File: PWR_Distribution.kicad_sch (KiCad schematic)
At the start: 39 parts, among them IC4 AP64501QSP-13, J1 CarPowerConnector, U7 LM76202QPWPRQ1

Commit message: small changes for ravi
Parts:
- removed C36, C37, C38, C39, C40, C41: 10u 35v, Capacitor_SMD:C_0805_2012Metric, symbol Device:C
- D10: value 3.3V -> 5V
- D11: Color Green -> Red; Inventory Y -> (none); Mouser Part Number 604-APTD2012LCGCK -> 604-APTD2012LSURCK; Mouser Price/Stock https://www.mouser.com/ProductDetail/Kingbright/APTD2012LCG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 -> https://www.mouser.com/ProductDetail/Kingbright/APTD2012LSU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; P/N APTD2012LCGCK -> APTD2012LSURCK; Vf 1.9V -> 1.75V
- R45: value 2.2k -> 1.5 k
- R46: value 5k -> 5.5k
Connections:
- net GNDPWR is gone; now on net GND: J1.2 (GND)
- net +5V_PWR: no longer R41.1
- net 12V_Extn renamed +12V_EXT
- net +12V_EXT: now also R41.1

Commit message: some stuff
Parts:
- C14: value 47uF -> 10u; P/N (none) -> TMK212BBJ106MGHT
- C54: value 100nF -> 100n; Mouser Part Number 80-C0805C104M5R -> (none)
- C55: value 47uF -> 10u
- D3: Mouser Part Number 771-PESD15VL1BA-T/R -> (none); Mouser Price/Stock https://www.mouser.com/ProductDetail/Nexperia/PESD15VL1BA11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 -> (none)
- D9: value 12V -> 12V Green LED; If 2mA -> (none); Inventory Y -> (none); Mouser Part Number 604-APTD2012LCGCK -> (none); Mouser Price/Stock https://www.mouser.com/ProductDetail/Kingbright/APTD2012LCG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 -> (none); Vf 1.9V -> (none)
- R40: value 10K -> 1k; Mouser Part Number 71-CRCW080510K0FKEAC -> (none)
- R41: value 10K -> 10k; Mouser Part Number 71-CRCW080510K0FKEAC -> (none)
- R42, R7: Mouser Part Number 71-CRCW0805100KFKEAC -> (none)
- R43: value 7.5K -> 6.6k; Mouser Part Number 71-CRCW080510K0FKEAC -> (none); P/N CRCW080510K0FKEAC -> (none)
- R44: Inventory Y -> (none); Mouser Part Number 71-CRCW0805-22.1K-E3 -> (none); Mouser Price/Stock https://www.mouser.com/ProductDetail/Vishay-Dale/CRCW080522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 -> (none); P/N CRCW080522K1FKEA -> (none)
- R8: value 3k -> 200; P/N (none) -> CR0805-JW-201ELF
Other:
- note added: "Est. max power draw = 15W (pi) + 3 * (1.5W) (USB lines) + 1.5W (HDMI) + 0.6W (CAN) = 21.6W (rest of board draws negligible power)"

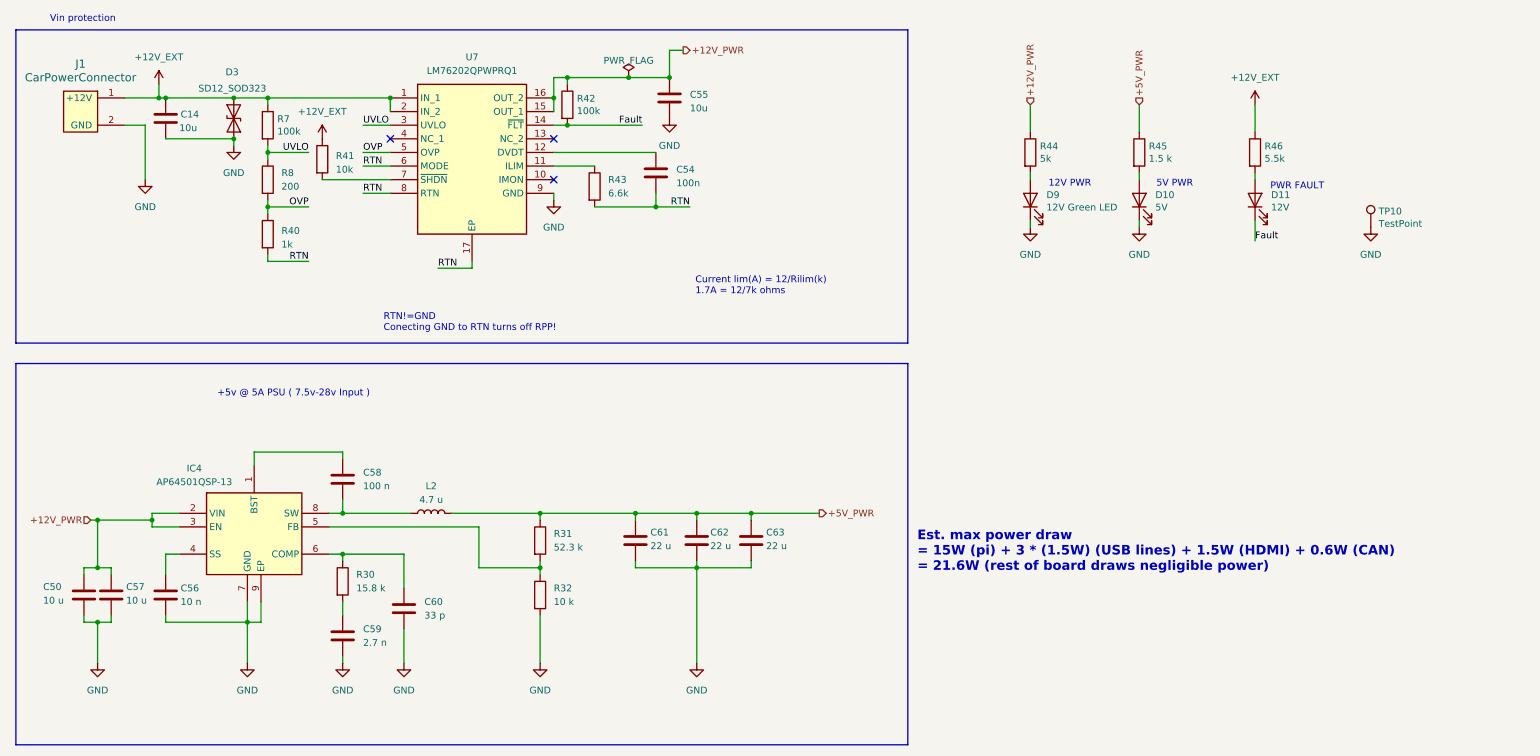
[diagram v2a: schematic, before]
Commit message: added parts to almost everything (except can xtal and fuses)
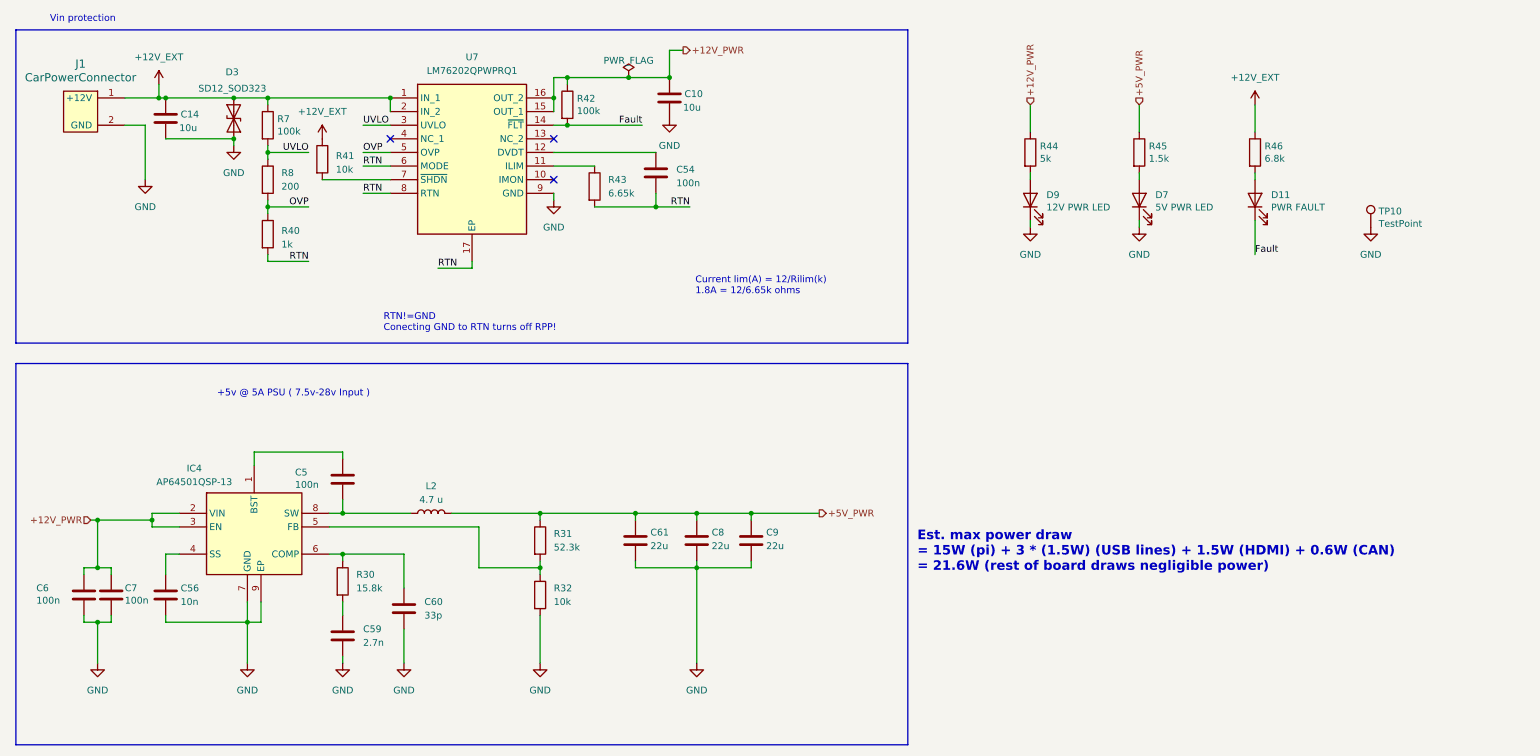
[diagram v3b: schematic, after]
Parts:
- removed C50, C57: 10 u, symbol Device:C
- removed C55: 10u, Capacitor_SMD:C_0805_2012Metric, symbol Device:C
- removed C58: 100 n, symbol Device:C
- removed C62, C63: 22 u, symbol Device:C
- removed D10: 5V, LED_SMD:LED_0805_2012Metric, symbol Device:LED
- added C10: 10u, Capacitor_SMD:C_0805_2012Metric, symbol Device:C
- added C5, C6, C7: 100n, Capacitor_SMD:C_0805_2012Metric, symbol Device:C
- added C8, C9: 22u, Capacitor_SMD:C_0805_2012Metric, symbol Device:C
- added D7: 5V PWR LED, LED_SMD:LED_0805_2012Metric, symbol Device:LED
- C56: value 10 n -> 10n; footprint (none) -> Capacitor_SMD:C_0805_2012Metric; P/N (none) -> C0805C103J5RACTU
- C59: value 2.7 n -> 2.7n; footprint (none) -> Capacitor_SMD:C_0805_2012Metric; P/N (none) -> VJ0805A272JXAAT
- C60: value 33 p -> 33p; footprint (none) -> Capacitor_SMD:C_0402_1005Metric; P/N (none) -> VJ0402A330JXACW1BC
- C61: value 22 u -> 22u; footprint (none) -> Capacitor_SMD:C_0805_2012Metric; P/N (none) -> CL21A226KQCLRNC
- D11: value 12V -> PWR FAULT; Color Red -> (none); If 2mA -> (none); Mouser Part Number 604-APTD2012LSURCK -> (none); Mouser Price/Stock https://www.mouser.com/ProductDetail/Kingbright/APTD2012LSU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 -> (none); Vf 1.75V -> (none)
- D9: value 12V Green LED -> 12V PWR LED; Color Green -> (none)
- IC4: footprint SOIC127P600X163-9N -> Controls_Pi:SOIC127P600X163-9N; Height 1.63 -> (none); Manufacturer_Name Diodes Incorporated -> (none); Manufacturer_Part_Number AP64501QSP-13 -> (none); Mouser Part Number 621-AP64501QSP-13 -> (none); Mouser Price/Stock https://www.mouser.co.uk/ProductDetail/Diodes-Incorporated/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 -> (none); P/N (none) -> AP64501QSP-13
- R30: value 15.8 k -> 15.8k; footprint (none) -> Resistor_SMD:R_0603_1608Metric; P/N (none) -> CRCW060315K8FKEAC
- R31: value 52.3 k -> 52.3k; footprint (none) -> Resistor_SMD:R_0603_1608Metric; P/N (none) -> CRCW060352K3FKEA
- R32: value 10 k -> 10k; footprint (none) -> Resistor_SMD:R_0805_2012Metric; P/N (none) -> CRCW080510K0FKEAC
- R43: value 6.6k -> 6.65k; P/N (none) -> CRCW12106K65FKEA
- R44: P/N (none) -> CRCW08055K00FKTA
- R45: value 1.5 k -> 1.5k; Mouser Part Number Inventory -> (none); P/N SDR10EZPF2200 -> SDR10EZPF1501
- R46: value 5.5k -> 6.8k; Inventory Y -> (none); Mouser Part Number 71-CRCW0805-22.1K-E3 -> (none); Mouser Price/Stock https://www.mouser.com/ProductDetail/Vishay-Dale/CRCW080522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 -> (none); P/N CRCW080522K1FKEA -> SDR10EZPF6801
- TP10: Field4 nf -> (none); Field5 nf -> (none); Field6 nf -> (none); Field7 nf -> (none)
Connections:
- net +12V_PWR: now also C10.1, C6.1, C7.1
- net +5V_PWR: now also C8.1, C9.1
- net GND: now also C10.2, C6.2, C7.2, C8.2, C9.2, D7.1 (K)
- net at R45.2: now also D7.2 (A)
- net at IC4.1 (BST): now also C5.1
- net at IC4.8 (SW), L2.1: now also C5.2
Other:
- note added: "Current lim(A) = 12/Rilim(k) 1.8A = 12/6.65k ohms"
- note removed: "12V PWR"
- note removed: "5V PWR"
- note removed: "Current lim(A) = 12/Rilim(k) 1.7A = 12/7k ohms"
- note removed: "PWR FAULT"

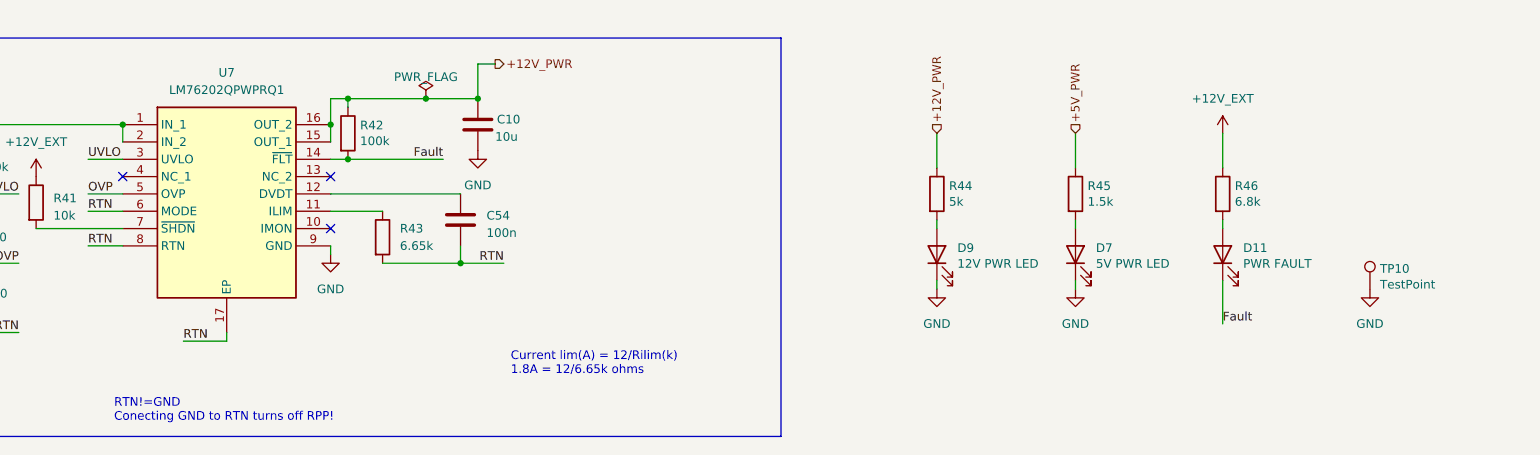
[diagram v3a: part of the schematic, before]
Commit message: fixed cap sizes, added remaining parts, fixed rtc battery
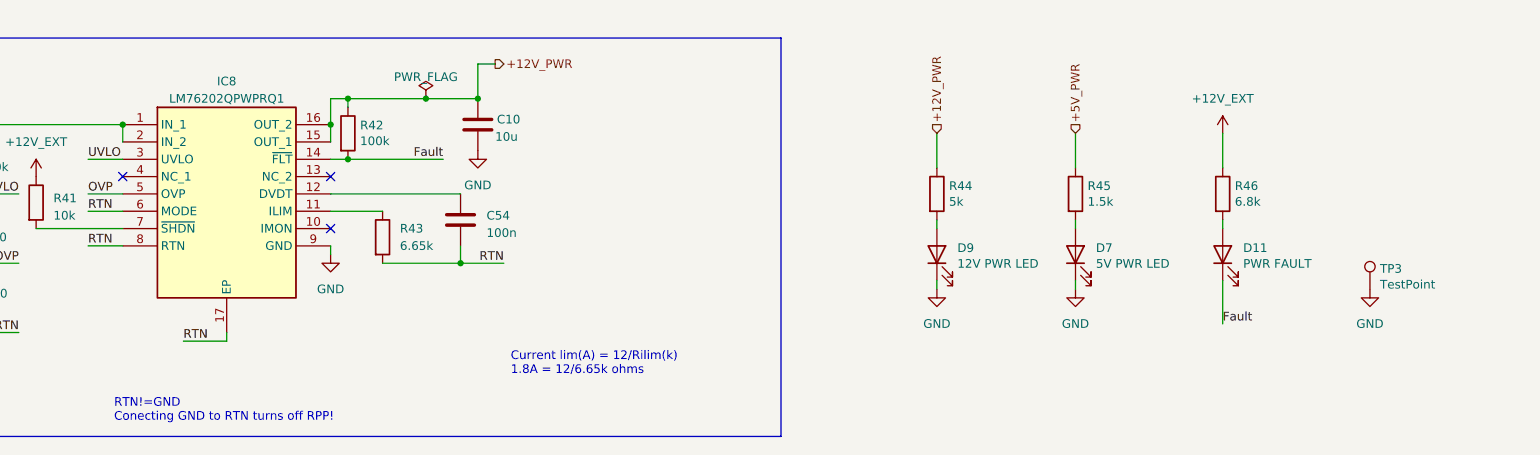
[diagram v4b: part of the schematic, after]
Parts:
- removed TP10: TestPoint, TestPoint:TestPoint_Pad_2.0x2.0mm, symbol Connector:TestPoint
- removed U7: LM76202QPWPRQ1, UTSVT_ICs:SOP65P640X120-17N, symbol utsvt-chips:LM76202QPWPRQ1
- added IC8: LM76202QPWPRQ1, Controls_Pi:SOP65P640X120-17N, symbol LM76202QPWPRQ1:LM76202QPWPRQ1
- added TP3: TestPoint, TestPoint:TestPoint_Pad_2.0x2.0mm, symbol Connector:TestPoint
- C60: footprint Capacitor_SMD:C_0402_1005Metric -> Capacitor_SMD:C_0805_2012Metric; P/N VJ0402A330JXACW1BC -> C0805C330J5RACTU
- IC4: Height (none) -> 1.63; Manufacturer_Name (none) -> Diodes Incorporated; Manufacturer_Part_Number (none) -> AP64501QSP-13; Mouser Part Number (none) -> 621-AP64501QSP-13; Mouser Price/Stock (none) -> https://www.mouser.co.uk/ProductDetail/Diodes-Incorporated/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
- J1: footprint (none) -> Connector_Molex:Molex_Micro-Fit_3.0_43650-0215_1x02_P3.00mm_Vertical; P/N (none) -> 436500215
- L2: footprint (none) -> Controls_Pi:INDPM110100X540N; P/N (none) -> SRP1050WA-4R7M
- R30: footprint Resistor_SMD:R_0603_1608Metric -> Resistor_SMD:R_0805_2012Metric; P/N CRCW060315K8FKEAC -> AA0805FR-0715K8L
- R31: footprint Resistor_SMD:R_0603_1608Metric -> Resistor_SMD:R_0805_2012Metric; P/N CRCW060352K3FKEA -> RC0805FR-0752K3L
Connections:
- net +12V_EXT: now also IC8.1 (IN_1), IC8.2 (IN_2)
- net +12V_PWR: now also IC8.15 (OUT_1), IC8.16 (OUT_2)
- net Fault: now also IC8.14 (~{FLT})
- net GND: now also IC8.9 (GND), TP3.1
- net OVP: now also IC8.5 (OVP)
- net RTN: now also IC8.17 (EP), IC8.6 (MODE), IC8.8 (RTN)
- net UVLO: now also IC8.3 (UVLO)
- net at R41.2: now also IC8.7 (~{SHDN})
- net at C54.1: now also IC8.12 (DVDT)
- net at R43.1: now also IC8.11 (ILIM)

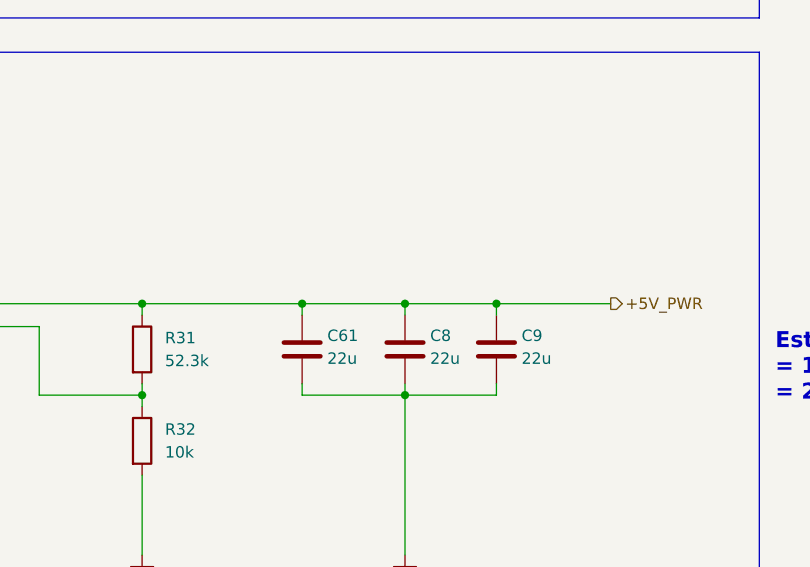
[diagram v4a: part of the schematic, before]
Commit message: fixed relevant erc errors
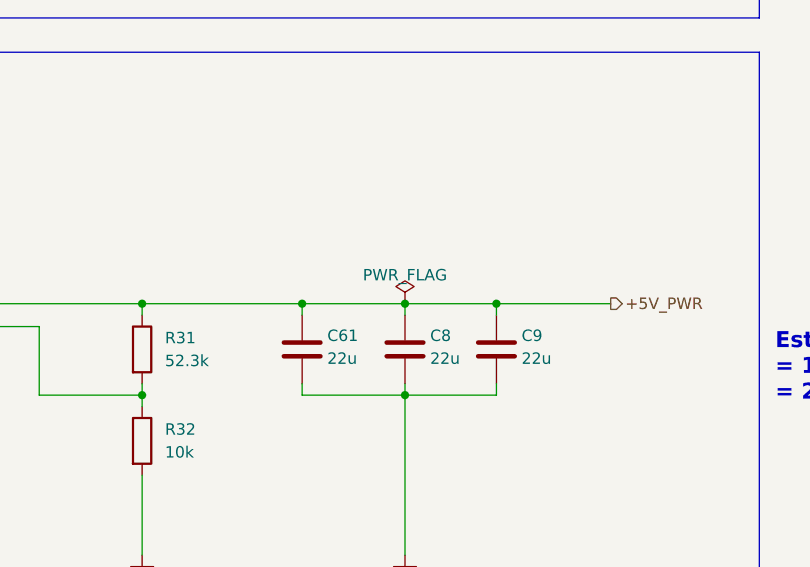
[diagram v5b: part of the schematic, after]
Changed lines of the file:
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@@
+	)
+	(symbol
+		(lib_id "power:PWR_FLAG")
+		(at 147.32 115.57 0)
+		(unit 1)
+		(exclude_from_sim no)
+		(in_bom yes)
+		(on_board yes)
+		(dnp no)
+		(fields_autoplaced yes)
+		(property "Reference" "#FLG02"
+			(at 147.32 113.665 0)
+			(effects
+				(font
+					(size 1.27 1.27)
+				)
+				(hide yes)
+			)
+		)
+		(property "Value" "PWR_FLAG"
+			(at 147.32 112.395 0)
+			(effects
+				(font
+					(size 1.27 1.27)
+				)
+			)
+		)
+		(property "Footprint" ""
+			(at 147.32 115.57 0)
+			(effects
+				(font
+					(size 1.27 1.27)
+				)
+				(hide yes)
+			)
+		)
+		(property "Datasheet" "~"
+			(at 147.32 115.57 0)
+			(effects
+				(font
+					(size 1.27 1.27)
+				)
+				(hide yes)
+			)
+		)
+		(property "Description" "Special symbol for telling ERC where power comes from"
+			(at 147.32 115.57 0)
+			(effects
+				(font
+					(size 1.27 1.27)
+				)
+				(hide yes)
+			)
+		)
+		(pin "1"
+		)
+		(instances
+			(project "PiBoard"
+				(path "/e4d65698-b8ec-4bf6-9f2b-a5010377155a/0c1fd794-8ba7-4f58-ad3e-1ee234c84a43"
+					(reference "#FLG02")
+					(unit 1)
+				)
+			)
+		)
 	)
 	(symbol

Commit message: moved some stuff around
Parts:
- R44: value 5k -> 10k
- R46: value 6.8k -> 12k
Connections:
- net +12V_EXT renamed +24V_EXT
- net +12V_PWR renamed +24V_PWR
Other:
- note added: "NEEDS TO CHANGE TO 24V"
- note added: "Should be ok for 24V?"
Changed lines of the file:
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@@
 		)
 	)
+	(text "Should be ok for 24V?"
+		(exclude_from_sim no)
+		(at 108.204 102.108 0)
+		(effects
+			(font
+				(size 2 2)
+				(thickness 0.4)
+				(bold yes)
+			)
+		)
+	)
 	(text "+5v @ 5A PSU ( 7.5v-28v Input )"
 		(exclude_from_sim no)
@@
 		)
 	)
+	(text "NEEDS TO CHANGE TO 24V"
+		(exclude_from_sim no)
+		(at 155.448 65.024 0)
+		(effects
+			(font
+				(size 2 2)
+				(thickness 0.4)
+				(bold yes)
+			)
+		)
+	)
 	(text "RTN!=GND \nConecting GND to RTN turns off RPP!"
 		(exclude_from_sim no)
@@
 		)
 	)
-	(hierarchical_label "+12V_PWR"
+	(hierarchical_label "+24V_PWR"
 		(shape input)
 		(at 209.55 39.37 90)
@@
 		)
 	)
-	(hierarchical_label "+12V_PWR"
+	(hierarchical_label "+24V_PWR"
 		(shape input)
 		(at 34.29 116.84 180)
@@
 		)
 	)
-	(hierarchical_label "+12V_PWR"
+	(hierarchical_label "+24V_PWR"
 		(shape output)
 		(at 144.78 29.21 0)
@@
 			)
 		)
-		(property "Value" "+12V_EXT"
-			(at 46.99 30.48 0)
+		(property "Value" "+24V_EXT"
+			(at 49.53 34.2899 0)
 			(effects
 				(font
 					(size 1.27 1.27)
 				)
+				(justify left)
 			)
 		)
@@
 			)
 		)
-		(property "Value" "5k"
+		(property "Value" "10k"
 			(at 211.328 49.403 0)
 			(effects
@@
 			)
 		)
-		(property "Value" "+12V_EXT"
+		(property "Value" "+24V_EXT"
 			(at 77.47 40.64 0)
 			(effects
@@
 			)
 		)
-		(property "Value" "6.8k"
+		(property "Value" "12k"
 			(at 253.238 49.403 0)
 			(effects
@@
 			)
 		)
-		(property "Value" "+12V_EXT"
+		(property "Value" "+24V_EXT"
 			(at 251.46 34.29 0)
 			(effects
